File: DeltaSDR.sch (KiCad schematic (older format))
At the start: 48 parts, among them J1 Conn_01x03_Male, J2 Conn_01x05_Male, J3 Barrel_Jack, J4 USB_A, U1 TC1262-33, U2 Si570, U4 PCM3060, U5 CY8C3246PVI-147, U6 TLV761, U7 TLV761, U8 74HC74, Y1 Crystal_GND24

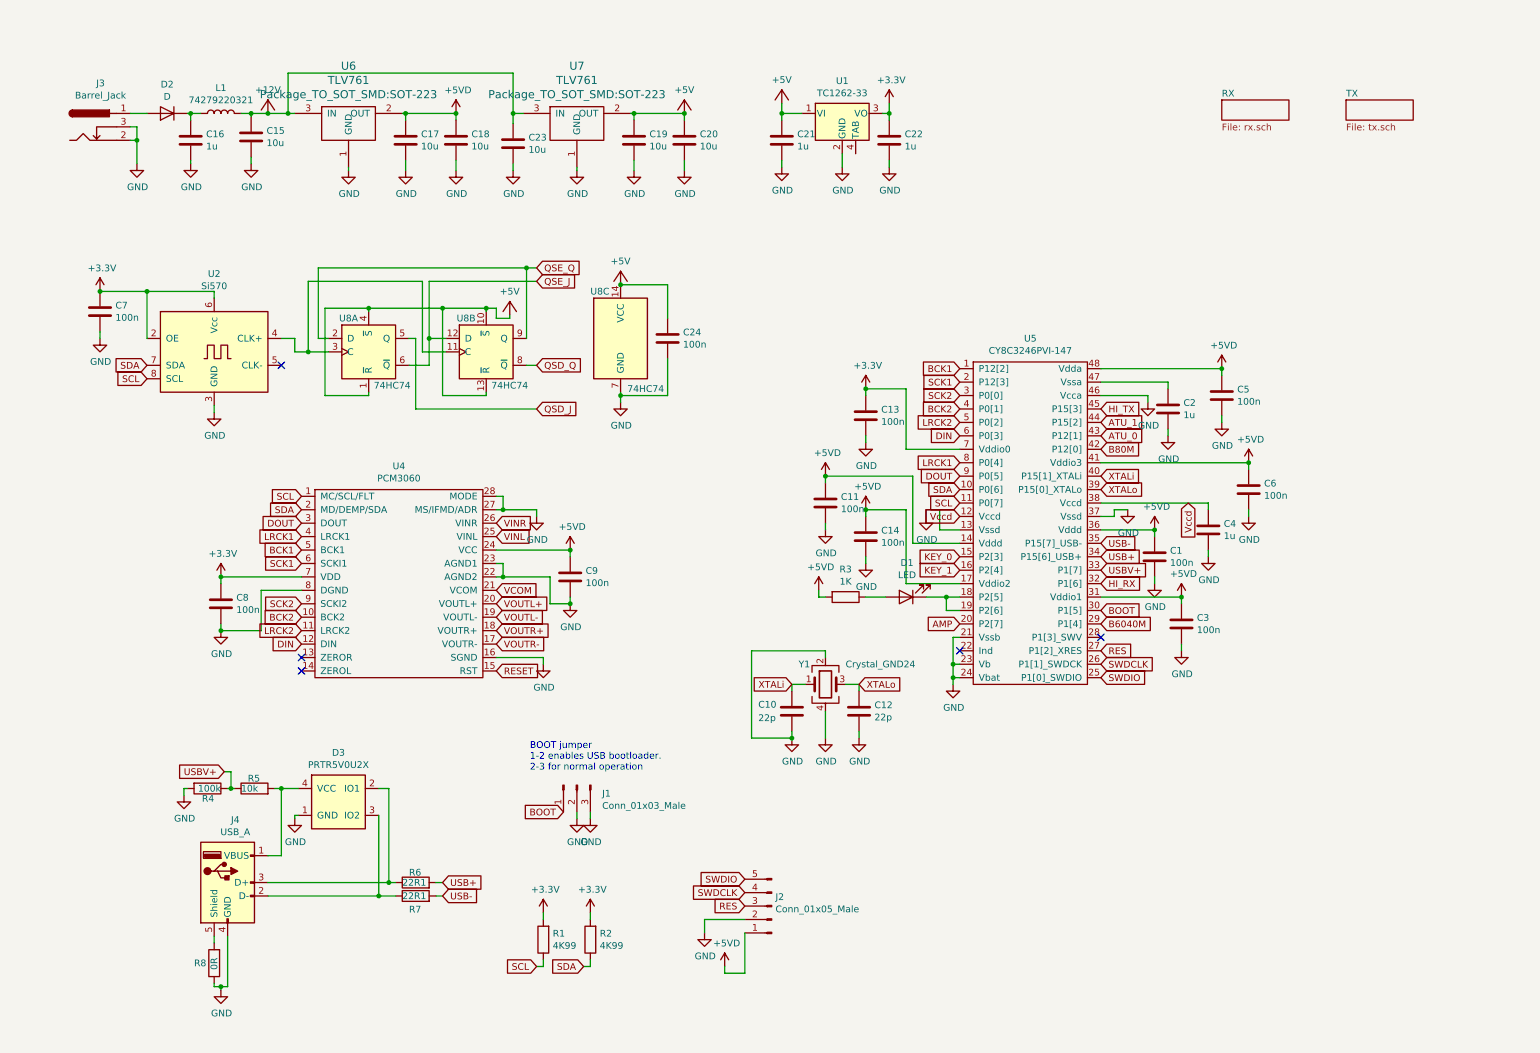
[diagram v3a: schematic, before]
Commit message: Changed board size, changed PA_IN signal position, changed LDOs, added 50 ohm tracks andvias
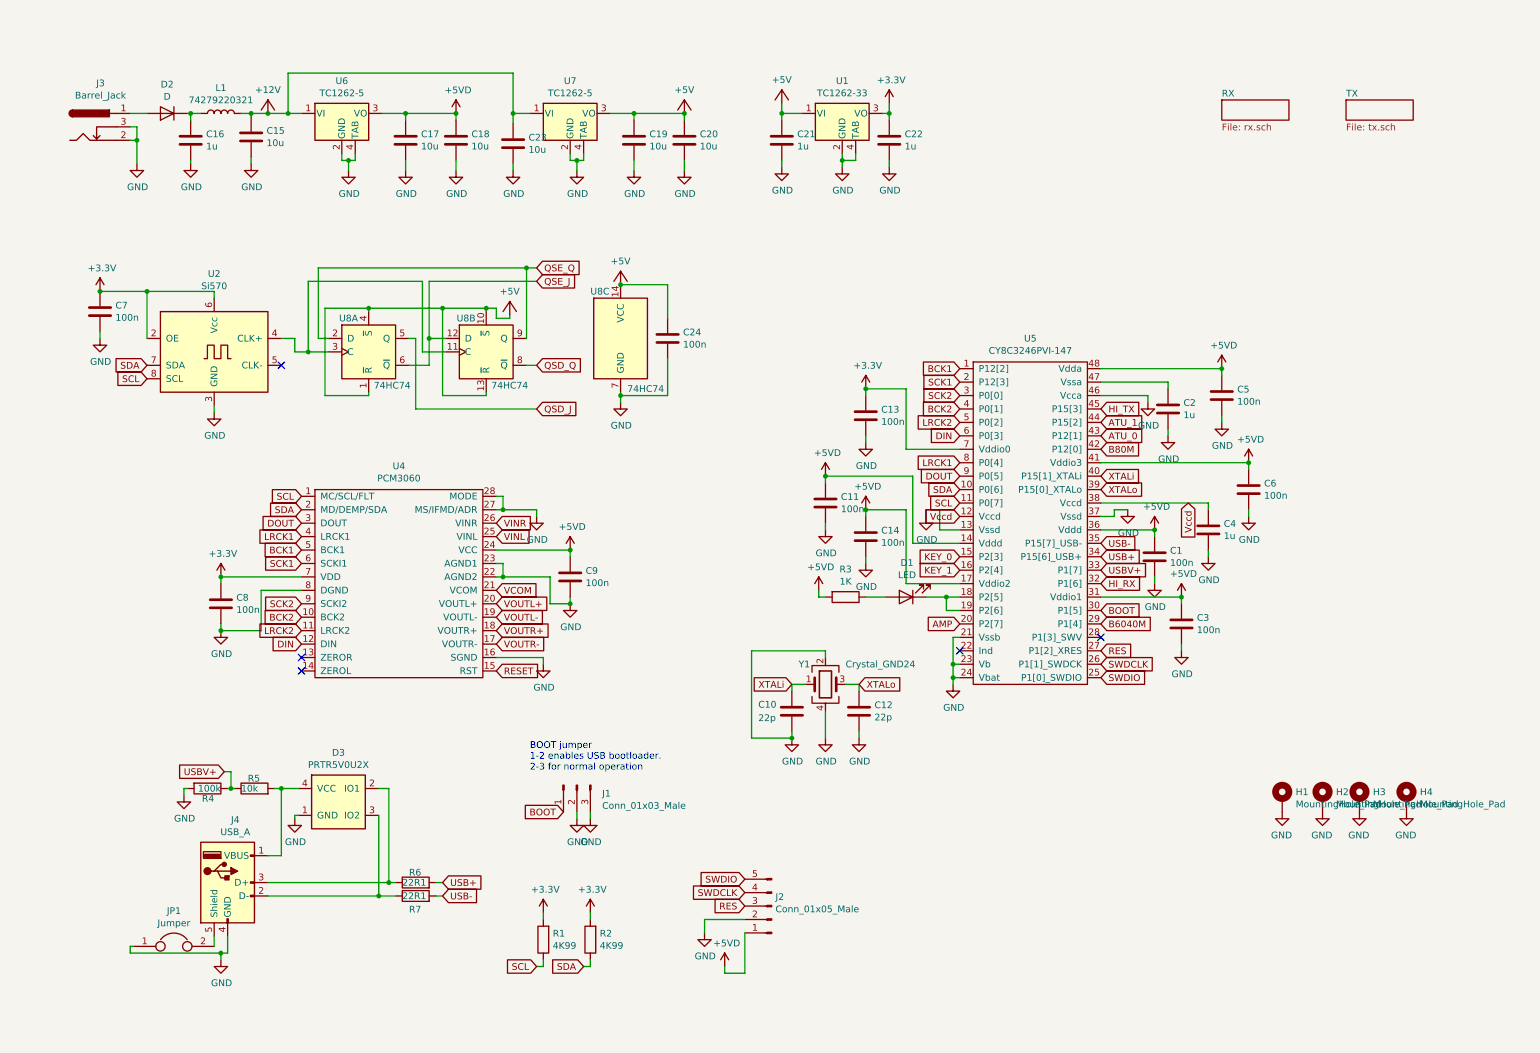
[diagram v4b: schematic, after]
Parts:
- removed R8: 0R, Resistor_SMD:R_0603_1608Metric, symbol DeltaSDR-rescue:R-Device-DeltaSDR-rescue
- removed U6, U7: TLV761, Package_TO_SOT_SMD:SOT-223, symbol DeltaSDR-rescue:LM1117-MLAB_U
- added H1, H2, H3, H4: MountingHole_Pad, MountingHole:MountingHole_3.2mm_M3_Pad_Via, symbol Mechanical:MountingHole_Pad
- added JP1: Jumper, Jumper:SolderJumper-2_P1.3mm_Open_RoundedPad1.0x1.5mm, symbol Device:Jumper
- added U6, U7: TC1262-5, Package_TO_SOT_SMD:SOT-223, symbol DeltaSDR-rescue:TC1262-33-regul
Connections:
- net +12V: now also U6.1 (VI), U7.1 (VI)
- net +5V: now also U7.3 (VO)
- net +5VD: now also U6.3 (VO)
- net GND: now also U1.4 (TAB), H1.1, H2.1, H3.1, H4.1, JP1.1, U6.2 (GND), U6.4 (TAB), U7.2 (GND), U7.4 (TAB)
- net at J4.5 (Shield): now also JP1.2
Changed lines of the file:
@@
 $EndComp
 Wire Wire Line
-	6675 1250 6675 1350
+	6675 1250 6675 1300
 Wire Wire Line
 	7025 1300 7025 1350
@@
 L power:GND #PWR0154
 U 1 1 5EA134A4
-P 2050 7475
-F 0 "#PWR0154" H 2050 7225 50  0001 C CNN
-F 1 "GND" H 2055 7302 50  0000 C CNN
-F 2 "" H 2050 7475 50  0001 C CNN
-F 3 "" H 2050 7475 50  0001 C CNN
-	1    2050 7475
+P 2050 7250
+F 0 "#PWR0154" H 2050 7000 50  0001 C CNN
+F 1 "GND" H 2055 7077 50  0000 C CNN
+F 2 "" H 2050 7250 50  0001 C CNN
+F 3 "" H 2050 7250 50  0001 C CNN
+	1    2050 7250
 	1    0    0    -1
 $EndComp
@@
 Wire Wire Line
 	3225 6775 2400 6775
-$Comp
-L DeltaSDR-rescue:R-Device-DeltaSDR-rescue R8
-U 1 1 5EA3C1AA
-P 2000 7275
-F 0 "R8" H 2150 7275 50  0000 R CNN
-F 1 "0R" V 2000 7325 50  0000 R CNN
-F 2 "Resistor_SMD:R_0603_1608Metric" V 1930 7275 50  0001 C CNN
-F 3 "~" H 2000 7275 50  0001 C CNN
-	1    2000 7275
-	-1   0    0    1
-$EndComp
-Wire Wire Line
-	2000 7075 2000 7125
-Wire Wire Line
-	2100 7075 2100 7450
-Wire Wire Line
-	2100 7450 2050 7450
-Wire Wire Line
-	2000 7450 2000 7425
-Wire Wire Line
-	2050 7475 2050 7450
-Connection ~ 2050 7450
-Wire Wire Line
-	2050 7450 2000 7450
 $Comp
 L DeltaSDR-rescue:R-Device-DeltaSDR-rescue R6
@@
 USB-
 $Comp
-L DeltaSDR-rescue:LM1117-MLAB_U U6
-U 1 1 5EA8F70D
-P 3000 1050
-F 0 "U6" H 3000 1503 60  0000 C CNN
-F 1 "TLV761" H 3000 1397 60  0000 C CNN
-F 2 "Package_TO_SOT_SMD:SOT-223" H 3000 1291 60  0000 C CNN
-F 3 "" H 3000 1050 60  0000 C CNN
-	1    3000 1050
-	1    0    0    -1
-$EndComp
-$Comp
 L power:GND #PWR0156
 U 1 1 5EA909BC
@@
 	2275 950  2400 950
 Connection ~ 2275 950
-Wire Wire Line
-	3000 1350 3000 1375
 $Comp
 L DeltaSDR-rescue:C-Device-DeltaSDR-rescue C17
@@
 $EndComp
 Wire Wire Line
-	3400 950  3425 950
-Wire Wire Line
 	3425 950  3425 1000
 Wire Wire Line
@@
 Connection ~ 3800 950
 $Comp
-L DeltaSDR-rescue:LM1117-MLAB_U U7
-U 1 1 5EADB5DF
-P 4700 1050
-F 0 "U7" H 4700 1503 60  0000 C CNN
-F 1 "TLV761" H 4700 1397 60  0000 C CNN
-F 2 "Package_TO_SOT_SMD:SOT-223" H 4700 1291 60  0000 C CNN
-F 3 "" H 4700 1050 60  0000 C CNN
-	1    4700 1050
-	1    0    0    -1
-$EndComp
-$Comp
 L power:GND #PWR0160
 U 1 1 5EADB5E9
@@
 	1    0    0    -1
 $EndComp
-Wire Wire Line
-	4700 1350 4700 1375
 $Comp
 L DeltaSDR-rescue:C-Device-DeltaSDR-rescue C19
@@
 $EndComp
 Wire Wire Line
-	5100 950  5125 950
-Wire Wire Line
 	5125 950  5125 1000
 Wire Wire Line
@@
 	4225 950  4225 1025
 Wire Wire Line
-	4225 950  4300 950
-Wire Wire Line
 	4225 1325 4225 1375
 Wire Wire Line
@@
 Connection ~ 4225 950
 Connection ~ 2550 950
-Wire Wire Line
-	2550 950  2600 950
 $Comp
 L DeltaSDR-rescue:+5V-mdSupply #PWR0164
@@
 Text GLabel 8600 4750 2    50   Input ~ 0
 B6040M
+$Comp
+L Device:Jumper JP1
+U 1 1 5EA337DB
+P 1700 7150
+F 0 "JP1" H 1700 7414 50  0000 C CNN
+F 1 "Jumper" H 1700 7323 50  0000 C CNN
+F 2 "Jumper:SolderJumper-2_P1.3mm_Open_RoundedPad1.0x1.5mm" H 1700 7150 50  0001 C CNN
+F 3 "~" H 1700 7150 50  0001 C CNN
+	1    1700 7150
+	1    0    0    -1
+$EndComp
+Wire Wire Line
+	2100 7075 2100 7200
+Wire Wire Line
+	2100 7200 2050 7200
+Wire Wire Line
+	2050 7200 2050 7250
+Wire Wire Line
+	2000 7075 2000 7150
+Wire Wire Line
+	1400 7150 1375 7150
+Wire Wire Line
+	1375 7150 1375 7200
+Wire Wire Line
+	1375 7200 2050 7200
+Connection ~ 2050 7200
+$Comp
+L Mechanical:MountingHole_Pad H?
+U 1 1 5EAFAA06
+P 10875 6050
+AR Path="/5E9BB9DC/5EAFAA06" Ref="H?"  Part="1"
+AR Path="/5EAFAA06" Ref="H4"  Part="1"
+F 0 "H4" H 10975 6099 50  0000 L CNN
+F 1 "MountingHole_Pad" H 10975 6008 50  0000 L CNN
+F 2 "MountingHole:MountingHole_3.2mm_M3_Pad_Via" H 10875 6050 50  0001 C CNN
+F 3 "~" H 10875 6050 50  0001 C CNN
+	1    10875 6050
+	1    0    0    -1
+$EndComp
+$Comp
+L power:GND #PWR0222
+U 1 1 5EAFAA0C
+P 10875 6150
+AR Path="/5EAFAA0C" Ref="#PWR0222"  Part="1"
+AR Path="/5E9BB9DC/5EAFAA0C" Ref="#PWR?"  Part="1"
+F 0 "#PWR0222" H 10875 5900 50  0001 C CNN
+F 1 "GND" H 10880 5977 50  0000 C CNN
+F 2 "" H 10875 6150 50  0001 C CNN
+F 3 "" H 10875 6150 50  0001 C CNN
+	1    10875 6150
+	-1   0    0    -1
+$EndComp
+$Comp
+L Mechanical:MountingHole_Pad H?
+U 1 1 5EAFAA12
+P 10525 6050
+AR Path="/5E9BB9DC/5EAFAA12" Ref="H?"  Part="1"
+AR Path="/5EAFAA12" Ref="H3"  Part="1"
+F 0 "H3" H 10625 6099 50  0000 L CNN
+F 1 "MountingHole_Pad" H 10625 6008 50  0000 L CNN
+F 2 "MountingHole:MountingHole_3.2mm_M3_Pad_Via" H 10525 6050 50  0001 C CNN
+F 3 "~" H 10525 6050 50  0001 C CNN
+	1    10525 6050
+	1    0    0    -1
+$EndComp
+$Comp
+L power:GND #PWR0223
+U 1 1 5EAFAA18
+P 10525 6150
+AR Path="/5EAFAA18" Ref="#PWR0223"  Part="1"
+AR Path="/5E9BB9DC/5EAFAA18" Ref="#PWR?"  Part="1"
+F 0 "#PWR0223" H 10525 5900 50  0001 C CNN
+F 1 "GND" H 10530 5977 50  0000 C CNN
+F 2 "" H 10525 6150 50  0001 C CNN
+F 3 "" H 10525 6150 50  0001 C CNN
+	1    10525 6150
+	-1   0    0    -1
+$EndComp
+$Comp
+L Mechanical:MountingHole_Pad H?
+U 1 1 5EAFAA1E
+P 10250 6050
+AR Path="/5E9BB9DC/5EAFAA1E" Ref="H?"  Part="1"
+AR Path="/5EAFAA1E" Ref="H2"  Part="1"
+F 0 "H2" H 10350 6099 50  0000 L CNN
+F 1 "MountingHole_Pad" H 10350 6008 50  0000 L CNN
+F 2 "MountingHole:MountingHole_3.2mm_M3_Pad_Via" H 10250 6050 50  0001 C CNN
+F 3 "~" H 10250 6050 50  0001 C CNN
+	1    10250 6050
+	1    0    0    -1
+$EndComp
+$Comp
+L power:GND #PWR0224
+U 1 1 5EAFAA24
+P 10250 6150
+AR Path="/5EAFAA24" Ref="#PWR0224"  Part="1"
+AR Path="/5E9BB9DC/5EAFAA24" Ref="#PWR?"  Part="1"
+F 0 "#PWR0224" H 10250 5900 50  0001 C CNN
+F 1 "GND" H 10255 5977 50  0000 C CNN
+F 2 "" H 10250 6150 50  0001 C CNN
+F 3 "" H 10250 6150 50  0001 C CNN
+	1    10250 6150
+	-1   0    0    -1
+$EndComp
+$Comp
+L Mechanical:MountingHole_Pad H?
+U 1 1 5EAFAA2A
+P 9950 6050
+AR Path="/5E9BB9DC/5EAFAA2A" Ref="H?"  Part="1"
+AR Path="/5EAFAA2A" Ref="H1"  Part="1"
+F 0 "H1" H 10050 6099 50  0000 L CNN
+F 1 "MountingHole_Pad" H 10050 6008 50  0000 L CNN
+F 2 "MountingHole:MountingHole_3.2mm_M3_Pad_Via" H 9950 6050 50  0001 C CNN
+F 3 "~" H 9950 6050 50  0001 C CNN
+	1    9950 6050
+	1    0    0    -1
+$EndComp
+$Comp
+L power:GND #PWR0225
+U 1 1 5EAFAA30
+P 9950 6150
+AR Path="/5EAFAA30" Ref="#PWR0225"  Part="1"
+AR Path="/5E9BB9DC/5EAFAA30" Ref="#PWR?"  Part="1"
+F 0 "#PWR0225" H 9950 5900 50  0001 C CNN
+F 1 "GND" H 9955 5977 50  0000 C CNN
+F 2 "" H 9950 6150 50  0001 C CNN
+F 3 "" H 9950 6150 50  0001 C CNN
+	1    9950 6150
+	-1   0    0    -1
+$EndComp
+Wire Wire Line
+	6775 1250 6775 1300
+Wire Wire Line
+	6775 1300 6675 1300
+Connection ~ 6675 1300
+Wire Wire Line
+	6675 1300 6675 1350
+$Comp
+L DeltaSDR-rescue:TC1262-33-regul U6
+U 1 1 5EB7A567
+P 2950 950
+F 0 "U6" H 2950 1192 50  0000 C CNN
+F 1 "TC1262-5" H 2950 1101 50  0000 C CNN
+F 2 "Package_TO_SOT_SMD:SOT-223" H 2950 1175 50  0001 C CIN
+F 3 "http://ww1.microchip.com/downloads/en/DeviceDoc/21373C.pdf" H 2950 650 50  0001 C CNN
+	1    2950 950
+	1    0    0    -1
+$EndComp
+$Comp
+L DeltaSDR-rescue:TC1262-33-regul U7
+U 1 1 5EB7AFAE
+P 4650 950
+F 0 "U7" H 4650 1192 50  0000 C CNN
+F 1 "TC1262-5" H 4650 1101 50  0000 C CNN
+F 2 "Package_TO_SOT_SMD:SOT-223" H 4650 1175 50  0001 C CIN
+F 3 "http://ww1.microchip.com/downloads/en/DeviceDoc/21373C.pdf" H 4650 650 50  0001 C CNN
+	1    4650 950
+	1    0    0    -1
+$EndComp
+Wire Wire Line
+	4950 950  5125 950
+Wire Wire Line
+	4225 950  4350 950
+Wire Wire Line
+	4650 1250 4650 1300
+Wire Wire Line
+	4650 1300 4700 1300
+Wire Wire Line
+	4750 1300 4750 1250
+Wire Wire Line
+	4700 1300 4700 1375
+Connection ~ 4700 1300
+Wire Wire Line
+	4700 1300 4750 1300
+Wire Wire Line
+	2550 950  2650 950
+Wire Wire Line
+	3250 950  3425 950
+Wire Wire Line
+	2950 1250 2950 1300
+Wire Wire Line
+	2950 1300 3000 1300
+Wire Wire Line
+	3050 1300 3050 1250
+Wire Wire Line
+	3000 1300 3000 1375
+Connection ~ 3000 1300
+Wire Wire Line
+	3000 1300 3050 1300
 $EndSCHEMATC
